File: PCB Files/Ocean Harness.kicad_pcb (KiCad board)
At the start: 4 copper layers, 115.8 x 75.2 mm, 22 parts, among them J1 JAE DX07S024XJ1R1100, J3 Molex 0346910200, J4 Molex 0346910200, J5 Molex 0346910162, J6 Molex 0346910162, K1 G5V-2 DC12, U1 Vishay DG419LEDY-T1-GE4, U2 Vishay DG419LEDY-T1-GE4, U3 L78L12_SOT89

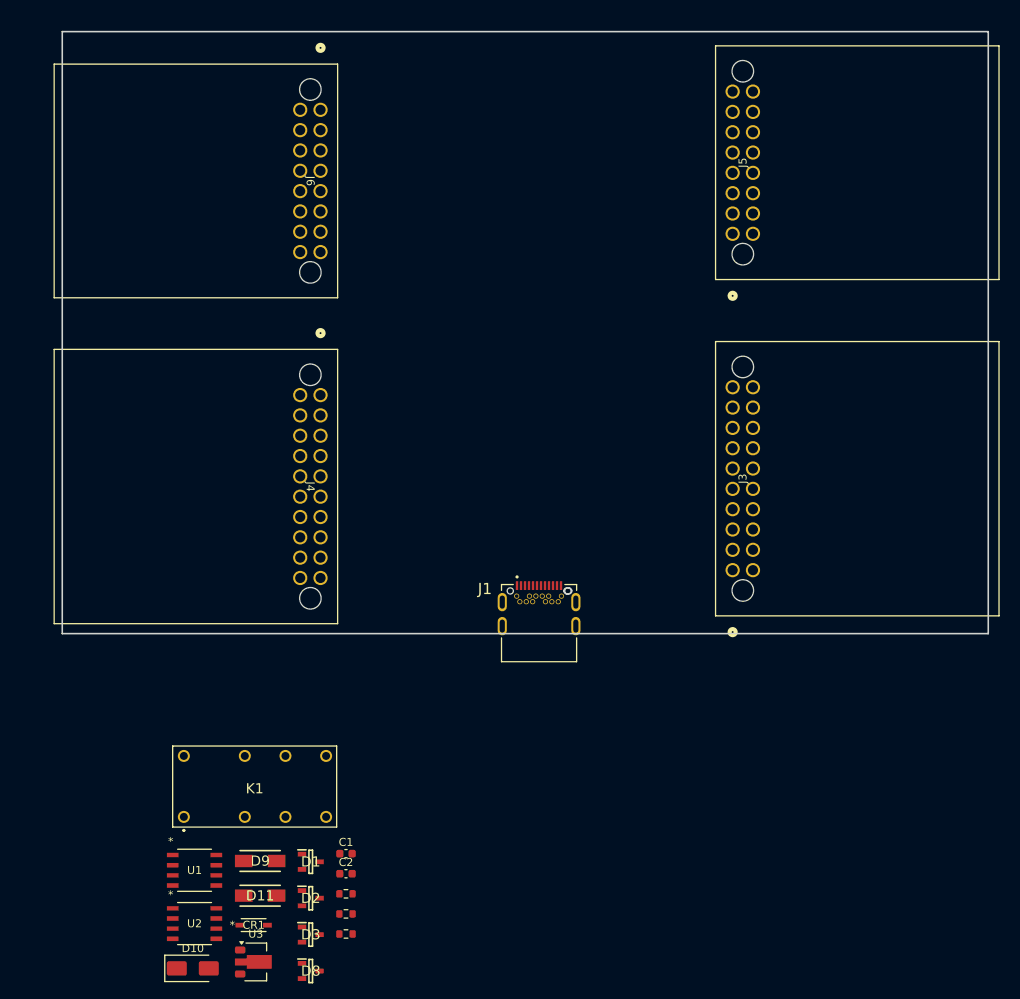
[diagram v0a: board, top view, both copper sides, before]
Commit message: Restructure to match passthrough-harness-box repo format; update board
Bring the repo in line with the volvo-polestar-passthrough-harness-box
layout: a 3D models/ directory with a render and STEP export, an
analysis/ manifest under PCB Files/, a dated design review, and a README
that describes the board rather than stubbing it.

Board changes made during the review, all with DRC and ERC at 0 errors:

- K1 changed to Omron G5V-2-H1 DC12 (960 R / 12.5 mA / 150 mW coil,
  180% max coil voltage). Package-identical to the G5V-2, so the
  footprint and 3D model carry over unchanged.
- U3 (L78L12) removed, replaced by R5 in the same footprint position.
  The part could never regulate: it needs >=14.5 V in and the DC-DC
  gives 13.4-14.1 V after the SS34 drop. R5 is 160 R, sized for the
  H1's 960 R coil.
- VBAT pass-through widened per segment, 61.4 mOhm -> 24.6 mOhm.
- Two M3 mounting holes added; the board previously had none.
- Redundant J1 Edge.Cuts cutout deleted, clearing 3 copper_edge_clearance
  errors. The library footprint still has the defect.
- 3D models added to J3/J4/J5/J6, sourced from Ocean Conversion PCB.

Co-Authored-By: Claude Opus 5 <noreply@anthropic.com>
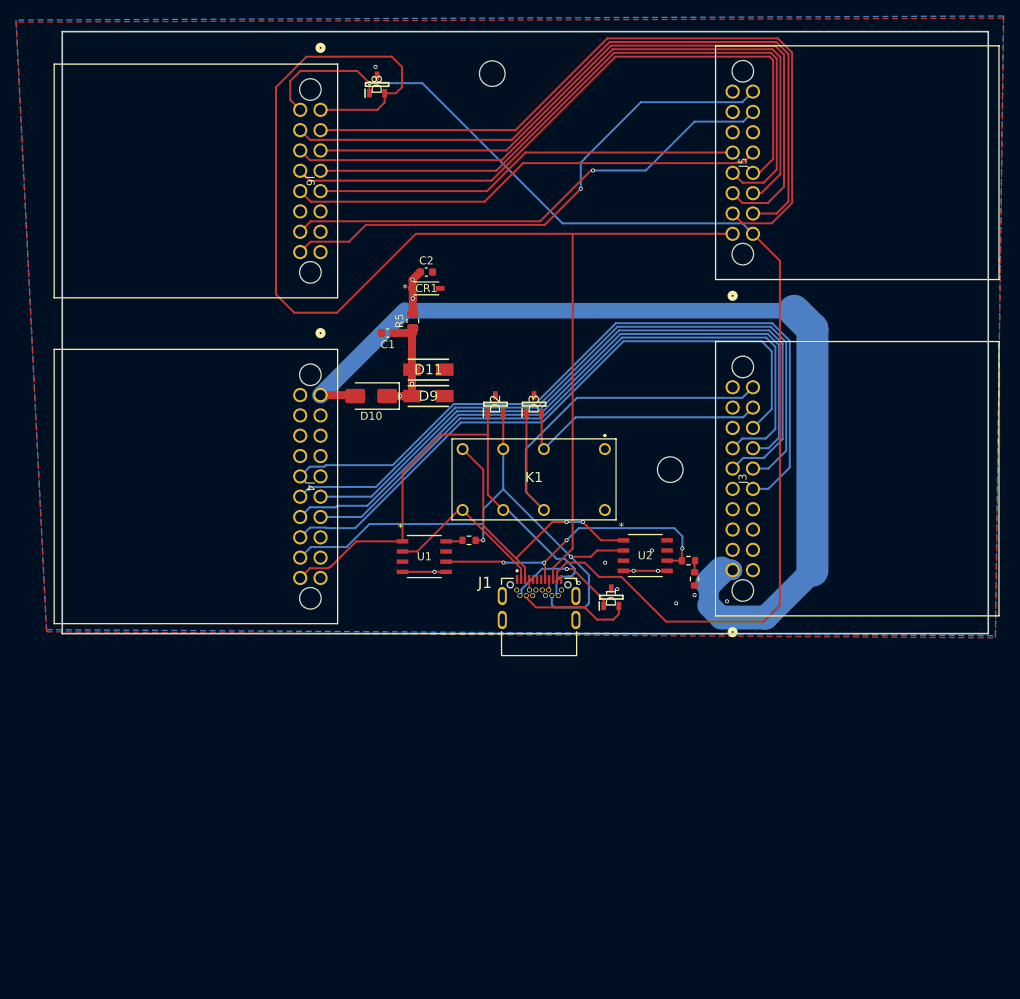
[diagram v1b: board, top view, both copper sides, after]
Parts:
- removed U3: L78L12_SOT89, Package_TO_SOT_SMD:SOT-89-3
- added H1: MountingHole_3.2mm_M3, MountingHole_3.2mm_M3, F.Cu at (136.0, 42.5)
- added H2: MountingHole_3.2mm_M3, MountingHole_3.2mm_M3, F.Cu at (158.2, 92.0)
- added R5: 160, R_0805_2012Metric, F.Cu at (126.1, 73.4)
- D9: value 16V -> SMAJ16A
- K1: value G5V-2 DC12 -> G5V-2-H1 DC12
- moved D8 111.1 mm to (121.6, 43.9), turned to 90 degrees
- moved CR1 82.5 mm to (127.8, 69.3)
- moved C2 75.9 mm to (127.8, 67.3)
- moved D10 74.9 mm to (120.9, 82.8), turned to 180 degrees
- moved U2 72.7 mm to (155.1, 102.7)
- moved D3 71.9 mm to (141.2, 83.8), turned to 90 degrees
- moved D11 69.0 mm to (128.0, 79.5)
- moved D2 65.9 mm to (136.4, 83.8), turned to 90 degrees
- moved C1 65.3 mm to (122.9, 74.9), turned to 180 degrees
- moved D9 61.8 mm to (128.0, 82.8)
- moved R3 60.4 mm to (161.3, 105.7), turned to -90 degrees
- moved R2 59.7 mm to (160.5, 103.4)
- moved K1 52.3 mm to (141.2, 93.0), turned to 180 degrees
- moved R4 51.6 mm to (133.1, 100.8)
- moved D1 50.1 mm to (150.9, 108.0), turned to 90 degrees
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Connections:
- J1 pad S2: (no net) -> GND
- J1 pad S3: (no net) -> GND
- J1 pad S4: (no net) -> GND
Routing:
- net /MRR_CAN_L: track 0.00 -> 164.7 mm
- net /MRR_CAN_H: track 0.00 -> 153.2 mm, vias 0 -> 1
- net /Harness_12v: track 0.00 -> 123.9 mm
- net /CMRR_FR_CAN_H: track 0.00 -> 92.2 mm
- net /USS1_PWR_N: track 0.00 -> 91.6 mm
- net /CMRR_FL_CAN_H: track 0.00 -> 90.7 mm
- net /USS1_Signal: track 0.00 -> 89.0 mm
- net /CMRR_FR_CAN_L: track 0.00 -> 88.1 mm
- net /USS2_PWR: track 0.00 -> 86.7 mm
- net /CMRR_FL_CAN_L: track 0.00 -> 85.7 mm
- net /USS2_Signal: track 0.00 -> 85.2 mm
- net /CMRR_RR_CAN_H: track 0.00 -> 84.0 mm
- net /USS1_PWR: track 0.00 -> 83.2 mm
- net /CMRR_RL_CAN_H: track 0.00 -> 81.8 mm
- net /USS2_PWR_N: track 0.00 -> 80.2 mm
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- added copper zone on In2.Cu, net /12V_PROT
- added copper zone on B.Cu, net GND
- added copper zone on F.Cu, net GND
- added copper zone on In1.Cu, net GND
- added copper zone on In2.Cu, net VIN
